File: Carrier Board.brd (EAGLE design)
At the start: 90 x 38.6 mm, 63 parts, among them J1 S2B-PH-SM4-TB(LF)(SN), J2 S2B-PH-SM4-TB(LF)(SN), J3 BM04B-SRSS-TB(LF)(SN), J4 BM06B-SRSS-TB(LF)(SN), J5 BM06B-SRSS-TB(LF)(SN), J6 BM06B-SRSS-TB(LF)(SN), J7 BM04B-SRSS-TB(LF)(SN), J8 BM04B-SRSS-TB(LF)(SN), J9 BM04B-SRSS-TB(LF)(SN), P1 Particle Boron / Xenon / Argon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

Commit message: Updated for Macrofab
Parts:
- removed H1, H2, H3, H4: STAND-OFF-M2.5, Custom Components:STAND-OFF-M2.5
- removed Q1: 2N7002L, Carrier Board:SOT23-3
- removed U2: MB85RC64, Fujitsu_By_element14_Batch_1:SOIC127P600X175-8N
- added Q2: BSS138, Custom Components:SOT-23_3L_ONS
- added U7: MB85RC64TA, Custom Components:SOIC127P600X175-8N
- C1, C10, C11, C2, C3, C4, C5, C6, C7, C9: device SparkFun-Capacitors:0805@1 -> Custom Components:0805@1
- F1: value 63V/1.5A -> 6V/0.5A
- J3, J7, J8, J9: value BM04B-SRSS-TB(LF)(SN) -> BM04B-SRSS-TBT(LF)(SN)
- J4, J5, J6: value BM06B-SRSS-TB(LF)(SN) -> BM06B-SRSS-TBT(LF)(SN)
- P1: device Carrier Board:PARTICLE-DEVICES_BORON -> Custom Components:PARTICLE-DEVICES_BORON
- R1, R4, R5, R6, R7, R8, R9: device SparkFun-Passives:0805 -> Custom Components:0805
- U1: device TMP36:RJ_5 -> Custom Components:RJ_5_ADI
- U3: device Carrier Board:QFN_16_ABR -> Custom Components:QFN_16_ABR
- U6: device Carrier Board:SOT-25_TOR -> Custom Components:SOT-25_TOR
- Y1: device Carrier Board:XTAL_ABS07-120-32.768KHZ-T -> Custom Components:XTAL_ABS07-120-32.768KHZ-T
- moved R5 5.18 mm to (7.11, 19.3)
- moved C1 3.42 mm to (11.2, 17.5), turned to 90 degrees
- moved R4 1.83 mm to (7.11, 21.1)
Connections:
- net 3V3R: now also U6.5; no longer U6.4
- net EN: now also Q2.3; no longer Q1.3
- net GND: now also Q2.2, U7.1, U7.2, U7.3, U7.4, U7.7; no longer Q1.2, U2.1, U2.2, U2.3, U2.4, U2.7
- net PSW: now also Q2.1; no longer Q1.1
- net SCL: now also U7.6; no longer U2.6
- net SDA: now also U7.5; no longer U2.5
- net VCC: now also U7.8; no longer U2.8
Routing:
- net VCC: track 106.1 -> 110.9 mm
- net SCL: track 91.6 -> 87.5 mm, vias 2 -> 3
- net SDA: track 92.6 -> 90.5 mm, vias 2 -> 1
- net 3V3R: track 32.2 -> 33.0 mm
- net GND: track 0.00 -> 0.27 mm, vias 61 -> 66

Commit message: Latest Version
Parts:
- C11: value 47pF -> GRM21A5C2D470JW01D; device Custom Components:0805@1 -> Custom Components:CAPC2012X100N
- J1, J2: value S2B-PH-SM4-TB(LF)(SN) -> B2B-PH-SM4-TB(LF)(SN); device SparkFun-Connectors:JST-2-SMD -> Custom Components:JST_B2B-PH-SM4-TB(LF)(SN)
- moved J2 19.1 mm to (78.5, 33.5)
- moved J1 18.3 mm to (59.4, 33.5)
- moved D3 1.61 mm to (69.3, 20.1), turned to 0 degrees
- moved JP7 0.51 mm to (73.7, 21.1)
- turned C11 to 270 degrees
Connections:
- net BATT-IN: now also J1.1; no longer J2.2
- net DC-IN: now also D3.C, J2.1; no longer J1.2, JP7.1
- net GND: now also C11.1, J1.2, J2.2, JP7.1; no longer C11.2, D3.A, J1.1, J2.1
- net N$1: now also D3.A; no longer D3.C
- net N$11: now also C11.2; no longer C11.1
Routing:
- net VCC2-EXT: track 54.8 -> 63.8 mm
- net SCL: track 87.5 -> 91.1 mm
- net DC-IN: track 20.7 -> 23.4 mm, vias 3 -> 1
- net N$1: track 5.19 -> 3.37 mm
- net GND: track 0.27 -> 1.81 mm, vias 66 -> 48
- net BATT-IN: track 39.4 -> 40.4 mm, vias 4 -> 2
- net SDA: track 90.5 -> 91.2 mm
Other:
- board text added: "Over Voltage Protection - JP7 must be closed for Argon Not required for Boron"
- board text added: "v1.6 - 1-11-21"
- board text removed: "Over Voltage Protection - JP7 must be closed for Argon & Xenon. Not required for Boron"
- board text removed: "v1.5- 11-2-20"

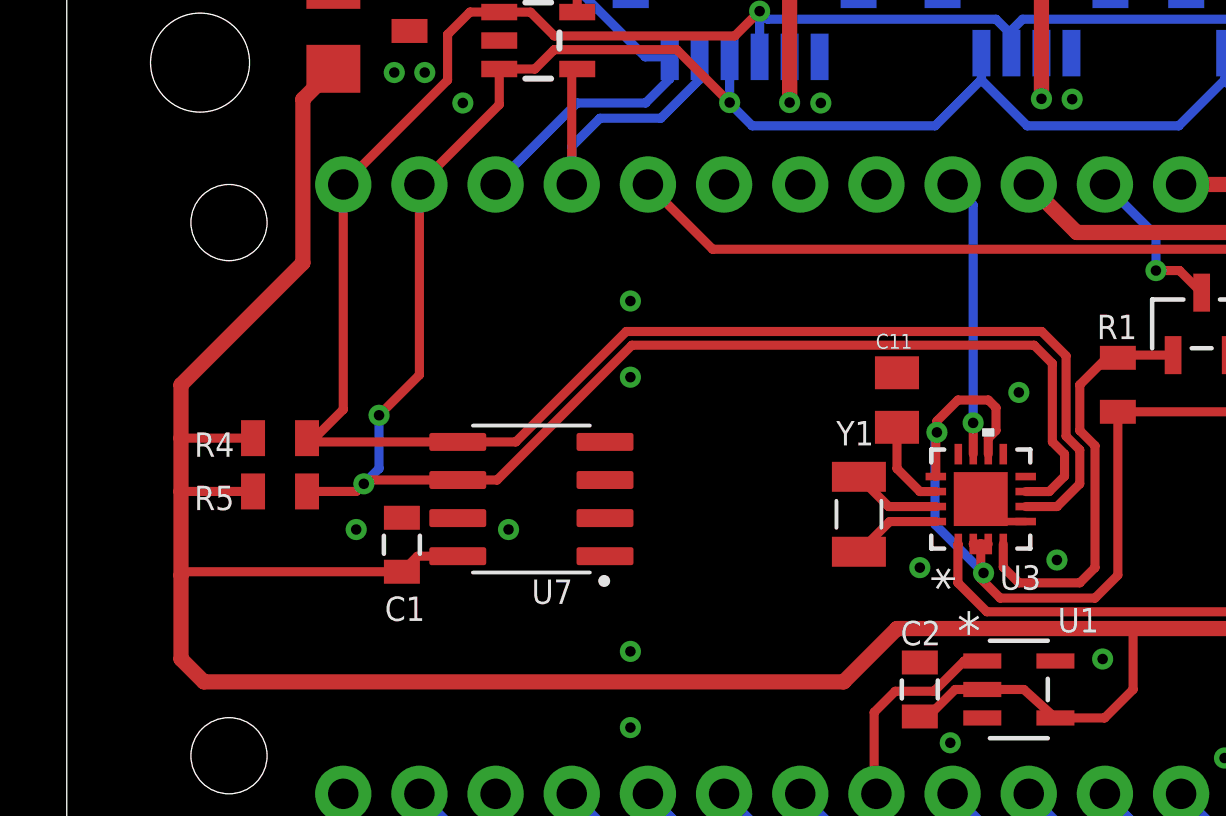
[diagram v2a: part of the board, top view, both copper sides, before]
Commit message: Updated FRAM footprint to address stock issue
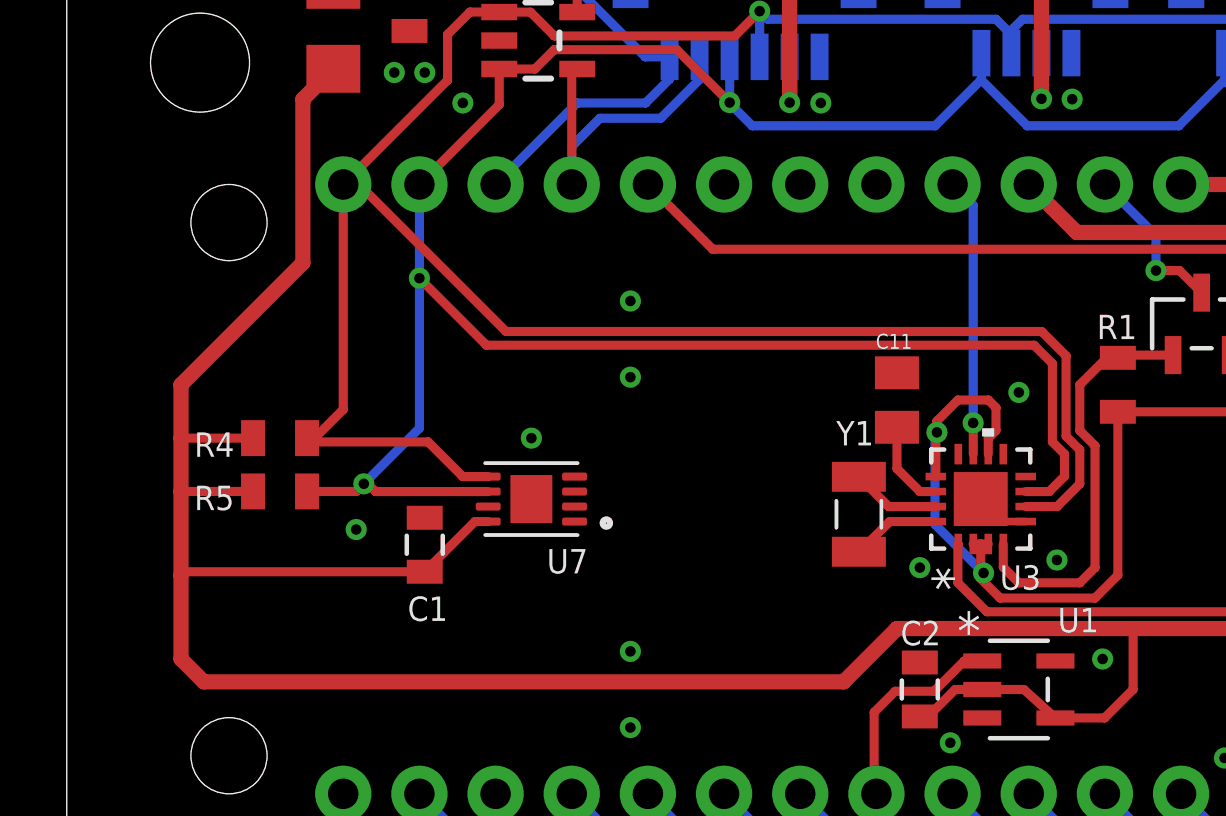
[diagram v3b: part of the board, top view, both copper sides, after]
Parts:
- U7: value MB85RC64TA -> MB85RC64TASON8; device Custom Components:SOIC127P600X175-8N -> Custom Components:SON50P200X300X75-9N
- moved C1 0.76 mm to (11.9, 17.5)
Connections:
- net GND: now also U7.9
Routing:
- net SDA: track 91.2 -> 97.0 mm
- net VCC: track 110.9 -> 112.4 mm
- net SCL: track 91.1 -> 92.5 mm
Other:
- board text added: "v1.6a - 3-29-21"
- board text removed: "v1.6 - 1-11-21"

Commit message: Fully functional
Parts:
- removed C5: 10nF, Custom Components:0805@1
- removed J3, J8: BM04B-SRSS-TBT(LF)(SN), Custom Components:CONN_BM04B-SRSS-TBT(LF)(SN)
- removed U4, U5: TPS22810, Custom Components:SOT-23-6
- added C12: 0.1uF, Custom Components:0805@1
- added FRAME4: FRAME-LETTERNO_PACKAGE, SparkFun-Aesthetics:DUMMY
- added J10: U.FL-R-SMT(10), Connectors:U.FL-R-SMT(10)
- added Q1, Q3: BSS215P, Custom Components:SOT-23_3L_ONS-M
- added R2, R3: 100k, Custom Components:0805
- added U2: RFM95CW-915S2, Custom Components:XCVR_RFM95W-868S2
- C4: value 10nF -> 10uF; device Custom Components:0805@1 -> Custom Components:C1206
- R8: value 100 -> 100k
- moved FRAME3 87.5 mm to (16.0, -26.7)
- moved R8 71.8 mm to (7.87, 14.7)
- moved C4 71.1 mm to (7.75, 23.4), turned to 0 degrees
- moved FRAME2 46.4 mm to (15.7, -51.7)
- moved FRAME1 31.3 mm to (16.0, -38.7)
- moved R9 12.6 mm to (73.2, 29.2), turned to 90 degrees
- moved C6 6.78 mm to (79.8, 18.8), turned to 0 degrees
- moved C7 6.62 mm to (64.0, 18.8), turned to 0 degrees
- moved F1 1.78 mm to (82.3, 22.4)
- moved Y1 0.92 mm to (26.9, 17.8)
- moved C11 0.72 mm to (27.2, 21.8)
- turned S1 to 270 degrees
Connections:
- removed net D2: G1.5, J4.6, P1.D2
- removed net EN/UVLO: C4.1, C5.1, S1.2, U4.3, U5.3
- removed net MD: P1.MD
- removed net N$10: C7.1, U4.4
- removed net N$6 (its old number): R8.1, U5.5
- removed net N$7: F1.1, R8.2, U5.6
- new net LORA-ANT: J10.SIG, U2.9
- new net ON/OFF: Q1.1, Q3.1, R2.1, S1.2
- new net RFM-INT: G1.5, J4.6, P1.D2, U2.14
- new net RFM-RST: P1.D6, R8.1, U2.6
- new net RFM-SS: P1.D5, R3.1, U2.5
- net BATT-IN: now also Q1.2; no longer U4.1
- net DC-IN: now also Q3.2; no longer U5.1
- net GND: now also C12.2, C4.P$2, J10.GND, J10.GND1, R9.1, U2.1, U2.10, U2.8; no longer C4.2, C5.2, J3.1, J3.SH1, J3.SH2, J8.1, J8.SH1, J8.SH2, S1.3, U4.2, U5.2
- net LI+: now also C7.1, Q1.3; no longer R9.2, U4.6
- net MISO: now also U2.2
- net MOSI: now also U2.3
- net N$12: now also R9.2, S1.3; no longer R9.1, U4.5
- net N$5: now also F1.1, Q3.3; no longer U5.4
- net N$9: now also R2.2
- net SCK: now also U2.4
- net SCL: no longer J3.4, J8.4
- net SDA: no longer J3.3, J8.3
- net VCC: now also C12.1, C4.P$1, R3.2, R8.2, U2.13
- net VCC2-EXT: no longer J3.2, J8.2
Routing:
- net EN/UVLO: track 44.8 -> 0.00 mm, vias 1 -> 0
- net RFM-INT: track 0.00 -> 37.5 mm, vias 0 -> 1
- net ON/OFF: track 0.00 -> 34.1 mm, vias 0 -> 1
- net RFM-RST: track 0.00 -> 33.6 mm, vias 0 -> 1
- net RFM-SS: track 0.00 -> 32.9 mm, vias 0 -> 1
- net VCC2-EXT: track 63.8 -> 37.3 mm, vias 4 -> 2
- net SCL: track 92.5 -> 70.1 mm
- net SDA: track 97.0 -> 77.6 mm
- net MISO: track 9.22 -> 26.7 mm
- net MOSI: track 7.99 -> 22.4 mm
- net D2: track 14.2 -> 0.00 mm, vias 1 -> 0
- net N$9: track 8.51 -> 21.1 mm, vias 1 -> 2
- net SCK: track 6.62 -> 19.1 mm
- net N$7: track 8.08 -> 0.00 mm
- net LI+: track 27.4 -> 35.2 mm
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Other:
- board text added: "LoRA"
- board text added: "Qwiic"
- board text added: "v1.7 - 4-28-21"
- board text removed: "Qwiic Connectors x3"
- board text removed: "v1.6a - 3-29-21"
